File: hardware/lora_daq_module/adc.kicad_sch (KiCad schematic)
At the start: 9 parts, among them J1 JST3pinfemale, U1 OPA333, U2 ADS1110A0IDBVR

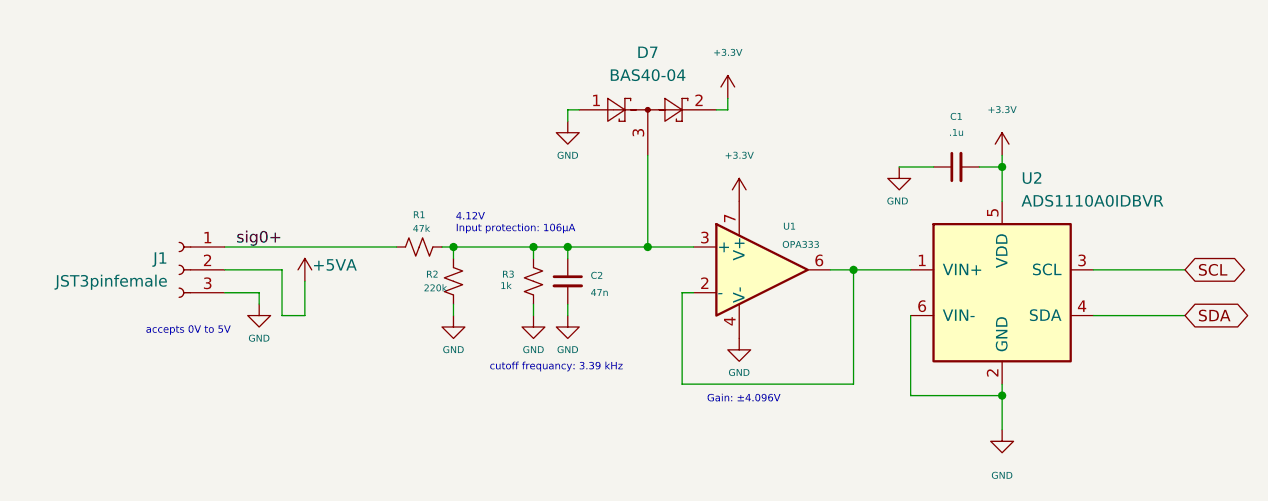
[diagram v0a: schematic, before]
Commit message: add test points and antenna microstrip
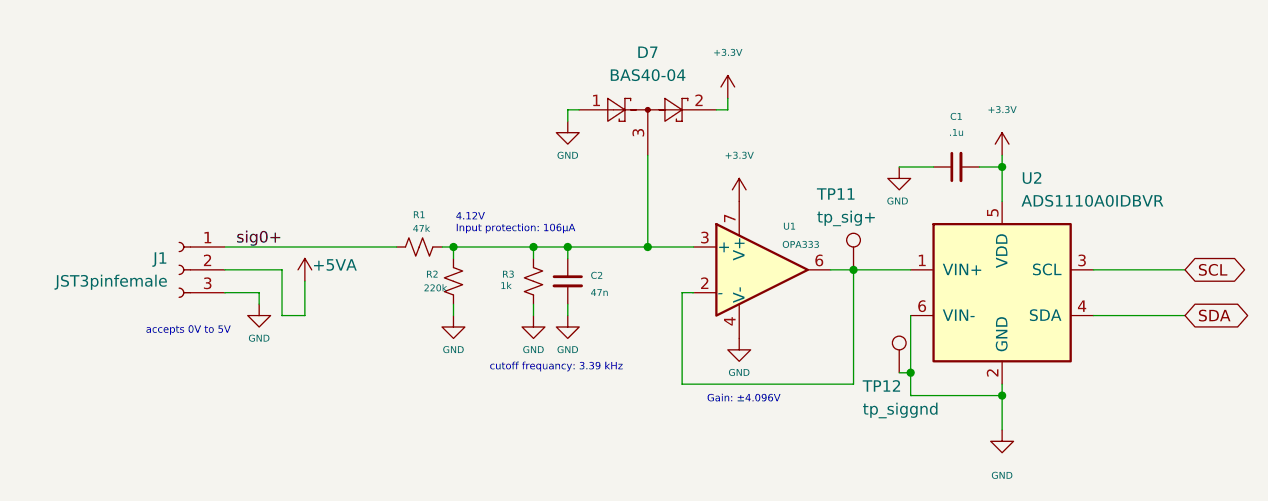
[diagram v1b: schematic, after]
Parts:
- added TP11: tp_sig+, TestPoint:TestPoint_THTPad_1.5x1.5mm_Drill0.7mm, symbol Connector:TestPoint
- added TP12: tp_siggnd, TestPoint:TestPoint_THTPad_1.5x1.5mm_Drill0.7mm, symbol Connector:TestPoint
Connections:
- net GND: now also TP12.1
- net at U1.2 (-), U1.6, U2.1 (VIN+): now also TP11.1
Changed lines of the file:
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@@
+	)
+	(junction
+		(at 176.53 115.57)
+		(diameter 0)
+		(color 0 0 0 0)
 	)
 	(junction
@@
 	(wire
 		(pts
-			(xy 176.53 109.22) (xy 176.53 118.11)
+			(xy 176.53 109.22) (xy 176.53 115.57)
 		)
 		(stroke
@@
 	(wire
 		(pts
+			(xy 175.26 115.57) (xy 176.53 115.57)
+		)
+		(stroke
+			(width 0)
+			(type default)
+		)
+	)
+	(wire
+		(pts
 			(xy 125.73 101.6) (xy 125.73 102.87)
 		)
@@
 		(pts
 			(xy 175.26 92.71) (xy 179.07 92.71)
+		)
+		(stroke
+			(width 0)
+			(type default)
+		)
+	)
+	(wire
+		(pts
+			(xy 176.53 115.57) (xy 176.53 118.11)
 		)
 		(stroke
@@
 	)
 	(symbol
+		(lib_id "Connector:TestPoint")
+		(at 170.18 104.14 0)
+		(unit 1)
+		(exclude_from_sim no)
+		(in_bom yes)
+		(on_board yes)
+		(dnp no)
+		(property "Reference" "TP11"
+			(at 166.116 95.758 0)
+			(effects
+				(font
+					(size 1.27 1.27)
+				)
+				(justify left)
+			)
+		)
+		(property "Value" "tp_sig+"
+			(at 166.116 98.298 0)
+			(effects
+				(font
+					(size 1.27 1.27)
+				)
+				(justify left)
+			)
+		)
+		(property "Footprint" "TestPoint:TestPoint_THTPad_1.5x1.5mm_Drill0.7mm"
+			(at 175.26 104.14 0)
+			(effects
+				(font
+					(size 1.27 1.27)
+				)
+				(hide yes)
+			)
+		)
+		(property "Datasheet" "~"
+			(at 175.26 104.14 0)
+			(effects
+				(font
+					(size 1.27 1.27)
+				)
+				(hide yes)
+			)
+		)
+		(property "Description" "test point"
+			(at 170.18 104.14 0)
+			(effects
+				(font
+					(size 1.27 1.27)
+				)
+				(hide yes)
+			)
+		)
+		(pin "1"
+		)
+		(instances
+			(project "lora_daq_module"
+				(path "/3a75d17e-6505-4097-95c7-feffd430343e/49d314b7-6ff8-4bd4-ae0d-0515c71c4ac4"
+					(reference "TP11")
+					(unit 1)
+				)
+			)
+		)
+	)
+	(symbol
 		(lib_id "power:GND")
 		(at 134.62 109.22 0)
@@
 					(unit 1)
 				)
+			)
+		)
+	)
+	(symbol
+		(lib_id "Connector:TestPoint")
+		(at 175.26 115.57 0)
+		(unit 1)
+		(exclude_from_sim no)
+		(in_bom yes)
+		(on_board yes)
+		(dnp no)
+		(property "Reference" "TP12"
+			(at 171.196 117.094 0)
+			(effects
+				(font
+					(size 1.27 1.27)
+				)
+				(justify left)
+			)
+		)
+		(property "Value" "tp_siggnd"
+			(at 171.196 119.634 0)
+			(effects
+				(font
+					(size 1.27 1.27)
+				)
+				(justify left)
+			)
+		)
+		(property "Footprint" "TestPoint:TestPoint_THTPad_1.5x1.5mm_Drill0.7mm"
+			(at 180.34 115.57 0)
+			(effects
+				(font
+					(size 1.27 1.27)
+				)
+				(hide yes)
+			)
+		)
+		(property "Datasheet" "~"
+			(at 180.34 115.57 0)
+			(effects
+				(font
+					(size 1.27 1.27)
+				)
+				(hide yes)
+			)
+		)
+		(property "Description" "test point"
+			(at 175.26 115.57 0)
+			(effects
+				(font
+					(size 1.27 1.27)
+				)
+				(hide yes)
+			)
+		)
+		(pin "1"
+		)
+		(instances
+			(project "lora_daq_module"
+				(path "/3a75d17e-6505-4097-95c7-feffd430343e/49d314b7-6ff8-4bd4-ae0d-0515c71c4ac4"
+					(reference "TP12")
+					(unit 1)
+				)

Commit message: add 0Ω resistors for disabling power circuits, revise adc input buffer and filter based on design review feedback, revise microstrip trace, add hardware reset button, add i2c connector and jst receptacle for battery
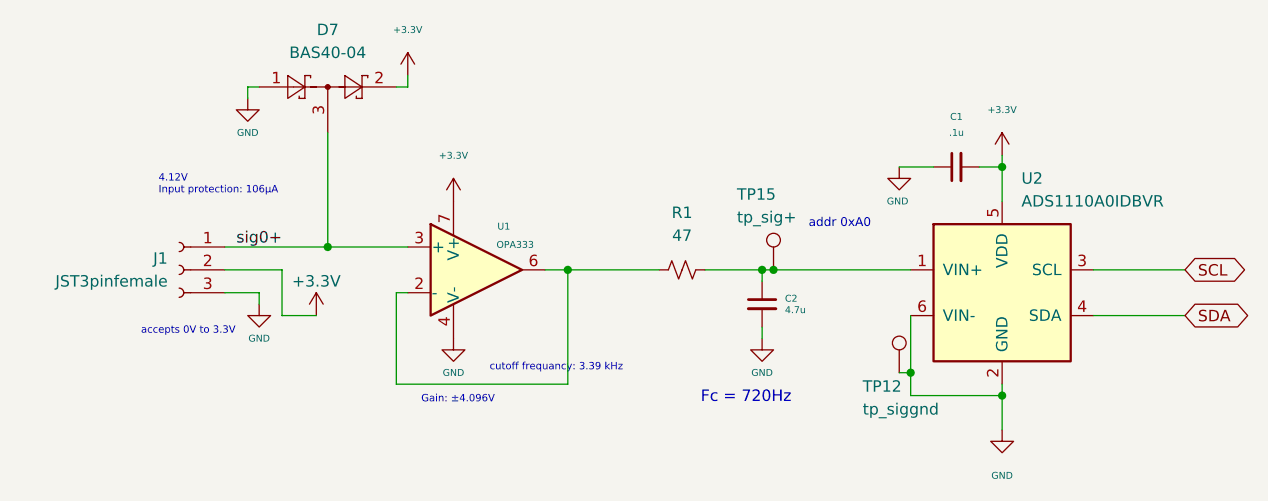
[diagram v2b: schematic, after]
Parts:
- removed R2: 220k, Resistor_SMD:R_0603_1608Metric, symbol Device:R_Small_US
- removed R3: 1k, Resistor_SMD:R_0603_1608Metric, symbol Device:R_Small_US
- removed TP11: tp_sig+, TestPoint:TestPoint_THTPad_1.5x1.5mm_Drill0.7mm, symbol Connector:TestPoint
- added TP15: tp_sig+, TestPoint:TestPoint_THTPad_1.5x1.5mm_Drill0.7mm, symbol Connector:TestPoint
- C2: value 47n -> 4.7u
- R1: value 47k -> 47; footprint Resistor_SMD:R_0603_1608Metric -> Resistor_SMD:R_1206_3216Metric; Desc 47 kOhms ±1% 0.1W, 1/10W Chip Resistor 0603 (1608 Metric) M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 -> 47 Ohms ±1% 0.25W, 1/4W Chip Resistor 1206 (3216 Metric) Mo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; Dist PN 311-47.0KHRCT-ND -> 311-47.0FRCT-ND; Mfr PN RC0603FR-0747KL -> RC1206FR-0747RL
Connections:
- net +5VA is gone; now on net +3.3V: J1.2 (Pin_2)
- net sig0+: now also D7.3, U1.3 (+); no longer R1.1
- net at C2.1, R1.2: now also U2.1 (VIN+), TP15.1; no longer D7.3, U1.3 (+)
- net at U1.2 (-), U1.6: now also R1.1; no longer U2.1 (VIN+)
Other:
- note added: "Fc = 720Hz"
- note added: "accepts 0V to 3.3V"
- note added: "addr 0xA0"
- note removed: "accepts 0V to 5V"
- moved on the sheet: C2, D7, U1
